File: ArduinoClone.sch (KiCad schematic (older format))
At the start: 13 parts, among them U1 DS1337, U2 24LC1025, U3 24LC1025, U4 ATMEGA328-AU, Y1 Crystal, Y2 Crystal

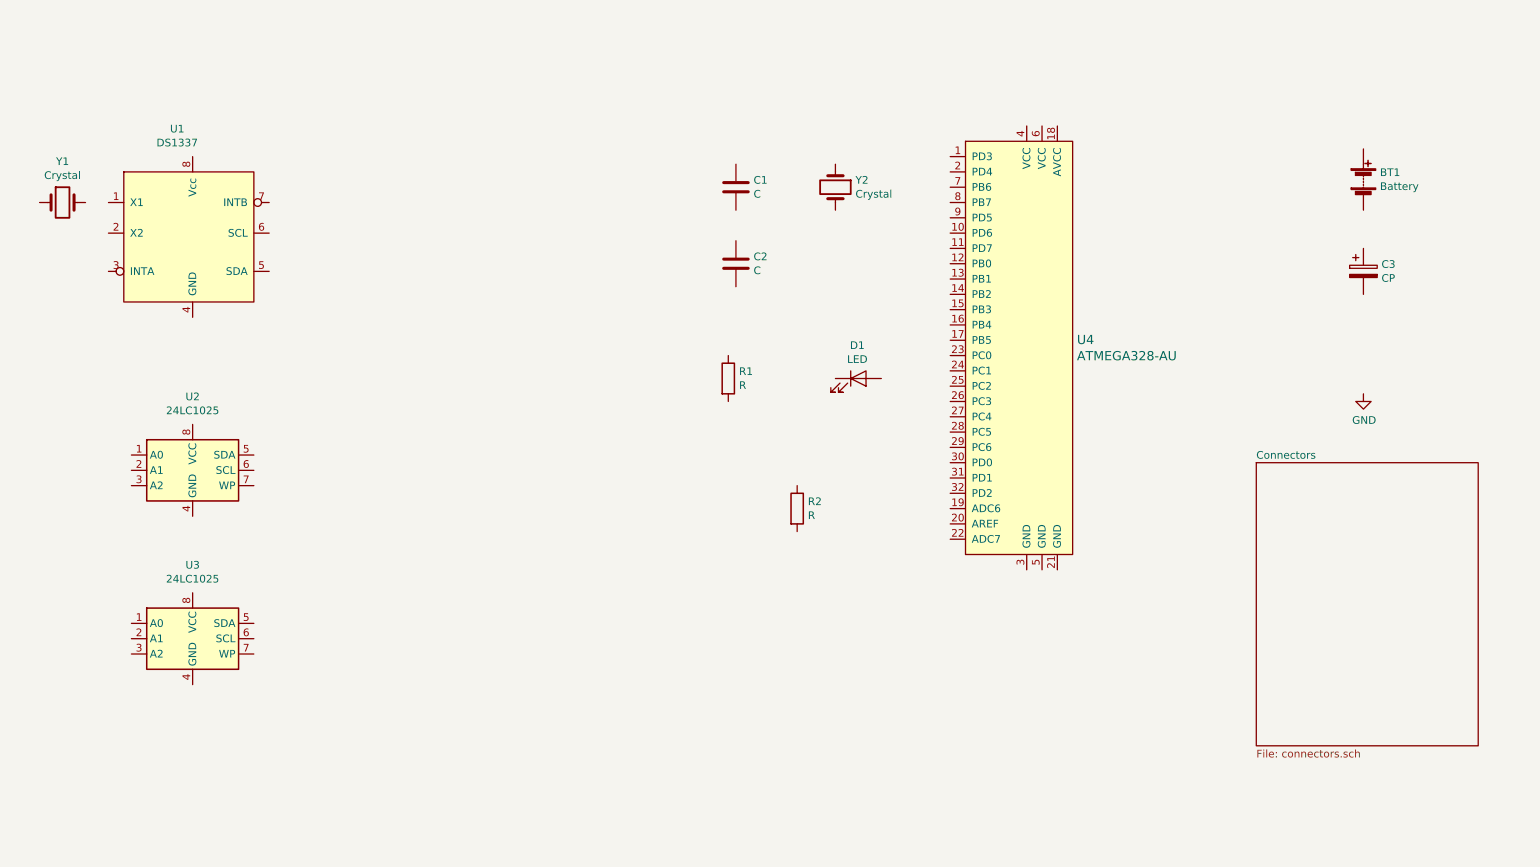
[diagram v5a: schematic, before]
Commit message: added components lables and footprints
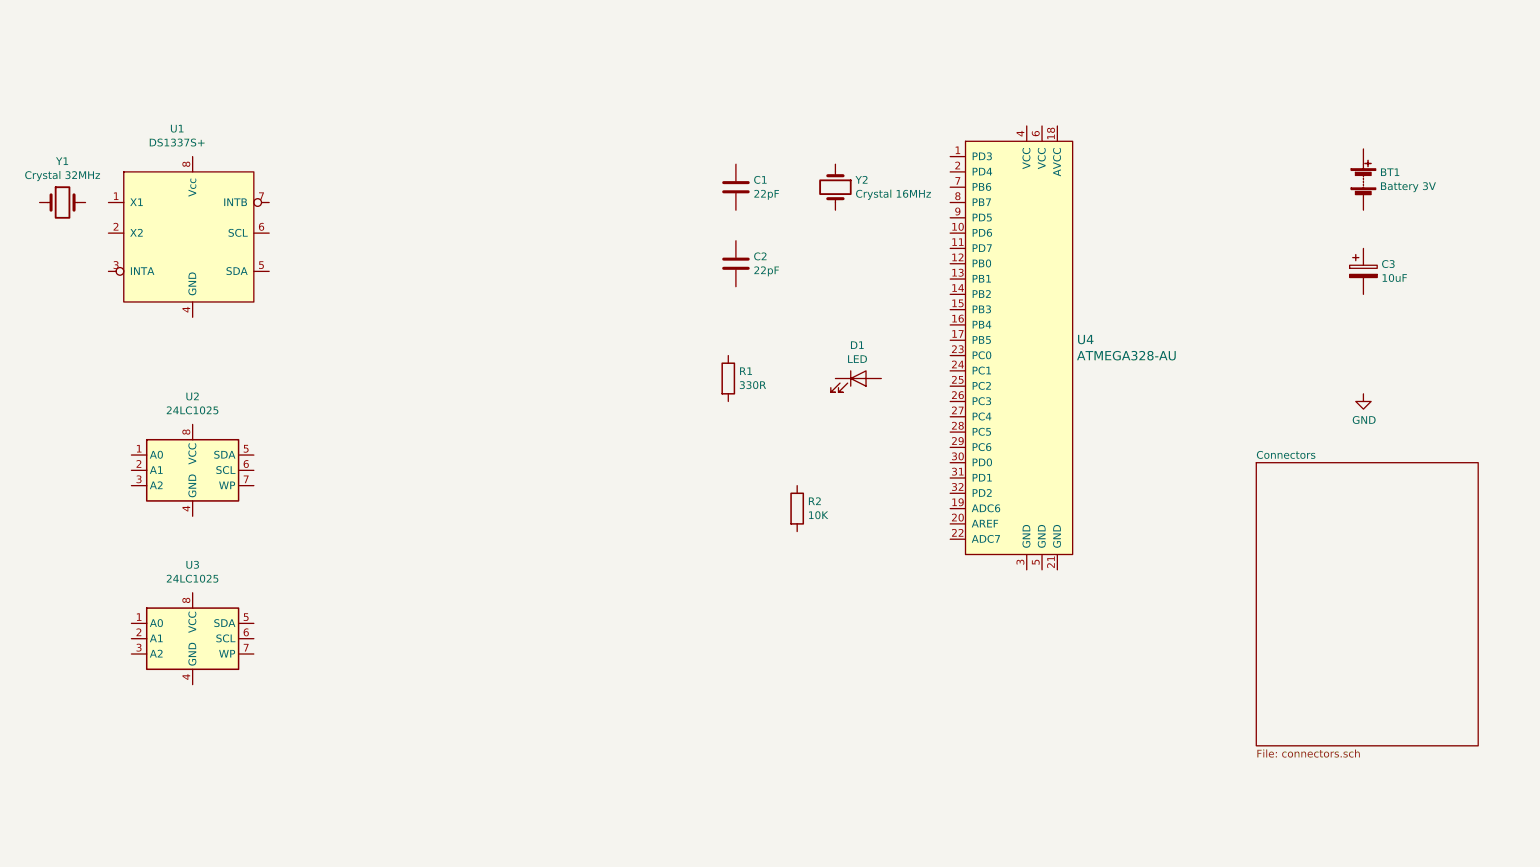
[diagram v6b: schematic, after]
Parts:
- BT1: value Battery -> Battery 3V; footprint (none) -> Connector_PinHeader_2.54mm:PinHeader_1x02_P2.54mm_Vertical
- C1, C2: value C -> 22pF; footprint (none) -> Capacitor_SMD:C_0805_2012Metric_Pad1.15x1.40mm_HandSolder
- C3: value CP -> 10uF; footprint (none) -> Capacitor_SMD:C_0805_2012Metric_Pad1.15x1.40mm_HandSolder
- D1: footprint (none) -> LED_SMD:LED_0805_2012Metric_Pad1.15x1.40mm_HandSolder
- R1: value R -> 330R; footprint (none) -> Resistor_SMD:R_0805_2012Metric_Pad1.15x1.40mm_HandSolder
- R2: value R -> 10K; footprint (none) -> Resistor_SMD:R_0805_2012Metric_Pad1.15x1.40mm_HandSolder
- U1: value DS1337 -> DS1337S+; footprint (none) -> Package_SO:SO-8_5.3x6.2mm_P1.27mm
- U2, U3: footprint (none) -> Package_SO:SOIJ-8_5.3x5.3mm_P1.27mm
- Y1: value Crystal -> Crystal 32MHz; footprint (none) -> Crystal:Crystal_SMD_MicroCrystal_CC7V-T1A-2Pin_3.2x1.5mm
- Y2: value Crystal -> Crystal 16MHz; footprint (none) -> Crystal:Crystal_SMD_5032-2Pin_5.0x3.2mm_HandSoldering
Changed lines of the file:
@@
 P 9650 2200
 F 0 "BT1" H 9758 2246 50  0000 L CNN
-F 1 "Battery" H 9758 2155 50  0000 L CNN
-F 2 "" V 9650 2260 50  0001 C CNN
+F 1 "Battery 3V" H 9758 2155 50  0000 L CNN
+F 2 "Connector_PinHeader_2.54mm:PinHeader_1x02_P2.54mm_Vertical" V 9650 2260 50  0001 C CNN
 F 3 "~" V 9650 2260 50  0001 C CNN
 	1    9650 2200
@@
 P 5550 2250
 F 0 "C1" H 5665 2296 50  0000 L CNN
-F 1 "C" H 5665 2205 50  0000 L CNN
-F 2 "" H 5588 2100 50  0001 C CNN
+F 1 "22pF" H 5665 2205 50  0000 L CNN
+F 2 "Capacitor_SMD:C_0805_2012Metric_Pad1.15x1.40mm_HandSolder" H 5588 2100 50  0001 C CNN
 F 3 "~" H 5550 2250 50  0001 C CNN
 	1    5550 2250
@@
 P 5550 2750
 F 0 "C2" H 5665 2796 50  0000 L CNN
-F 1 "C" H 5665 2705 50  0000 L CNN
-F 2 "" H 5588 2600 50  0001 C CNN
+F 1 "22pF" H 5665 2705 50  0000 L CNN
+F 2 "Capacitor_SMD:C_0805_2012Metric_Pad1.15x1.40mm_HandSolder" H 5588 2600 50  0001 C CNN
 F 3 "~" H 5550 2750 50  0001 C CNN
 	1    5550 2750
@@
 P 9650 2800
 F 0 "C3" H 9768 2846 50  0000 L CNN
-F 1 "CP" H 9768 2755 50  0000 L CNN
-F 2 "" H 9688 2650 50  0001 C CNN
+F 1 "10uF" H 9768 2755 50  0000 L CNN
+F 2 "Capacitor_SMD:C_0805_2012Metric_Pad1.15x1.40mm_HandSolder" H 9688 2650 50  0001 C CNN
 F 3 "~" H 9650 2800 50  0001 C CNN
 	1    9650 2800
@@
 F 0 "D1" H 6343 3716 50  0000 C CNN
 F 1 "LED" H 6343 3625 50  0000 C CNN
-F 2 "" H 6350 3500 50  0001 C CNN
+F 2 "LED_SMD:LED_0805_2012Metric_Pad1.15x1.40mm_HandSolder" H 6350 3500 50  0001 C CNN
 F 3 "~" H 6350 3500 50  0001 C CNN
 	1    6350 3500
@@
 P 5950 4350
 F 0 "R2" H 6020 4396 50  0000 L CNN
-F 1 "R" H 6020 4305 50  0000 L CNN
-F 2 "" V 5880 4350 50  0001 C CNN
+F 1 "10K" H 6020 4305 50  0000 L CNN
+F 2 "Resistor_SMD:R_0805_2012Metric_Pad1.15x1.40mm_HandSolder" V 5880 4350 50  0001 C CNN
 F 3 "~" H 5950 4350 50  0001 C CNN
 	1    5950 4350
@@
 P 5500 3500
 F 0 "R1" H 5570 3546 50  0000 L CNN
-F 1 "R" H 5570 3455 50  0000 L CNN
-F 2 "" V 5430 3500 50  0001 C CNN
+F 1 "330R" H 5570 3455 50  0000 L CNN
+F 2 "Resistor_SMD:R_0805_2012Metric_Pad1.15x1.40mm_HandSolder" V 5430 3500 50  0001 C CNN
 F 3 "~" H 5500 3500 50  0001 C CNN
 	1    5500 3500
@@
 F 0 "U2" H 2000 4581 50  0000 C CNN
 F 1 "24LC1025" H 2000 4490 50  0000 C CNN
-F 2 "" H 2000 4100 50  0001 C CNN
+F 2 "Package_SO:SOIJ-8_5.3x5.3mm_P1.27mm" H 2000 4100 50  0001 C CNN
 F 3 "http://ww1.microchip.com/downloads/en/DeviceDoc/21941B.pdf" H 2000 4100 50  0001 C CNN
 	1    2000 4100
@@
 P 2000 2550
 F 0 "U1" H 1899 3231 50  0000 C CNN
-F 1 "DS1337" H 1899 3140 50  0000 C CNN
-F 2 "" H 1900 2950 50  0001 C CNN
+F 1 "DS1337S+" H 1899 3140 50  0000 C CNN
+F 2 "Package_SO:SO-8_5.3x6.2mm_P1.27mm" H 1900 2950 50  0001 C CNN
 F 3 "" H 1900 2950 50  0001 C CNN
 	1    2000 2550
@@
 P 6200 2250
 F 0 "Y2" V 6154 2381 50  0000 L CNN
-F 1 "Crystal" V 6245 2381 50  0000 L CNN
-F 2 "" H 6200 2250 50  0001 C CNN
+F 1 "Crystal 16MHz" V 6245 2381 50  0000 L CNN
+F 2 "Crystal:Crystal_SMD_5032-2Pin_5.0x3.2mm_HandSoldering" H 6200 2250 50  0001 C CNN
 F 3 "~" H 6200 2250 50  0001 C CNN
 	1    6200 2250
@@
 P 1150 2350
 F 0 "Y1" H 1150 2618 50  0000 C CNN
-F 1 "Crystal" H 1150 2527 50  0000 C CNN
-F 2 "" H 1150 2350 50  0001 C CNN
+F 1 "Crystal 32MHz" H 1150 2527 50  0000 C CNN
+F 2 "Crystal:Crystal_SMD_MicroCrystal_CC7V-T1A-2Pin_3.2x1.5mm" H 1150 2350 50  0001 C CNN
 F 3 "~" H 1150 2350 50  0001 C CNN
 	1    1150 2350
@@
 F 0 "U3" H 2000 5681 50  0000 C CNN
 F 1 "24LC1025" H 2000 5590 50  0000 C CNN
-F 2 "" H 2000 5200 50  0001 C CNN
+F 2 "Package_SO:SOIJ-8_5.3x5.3mm_P1.27mm" H 2000 5200 50  0001 C CNN
 F 3 "http://ww1.microchip.com/downloads/en/DeviceDoc/21941B.pdf" H 2000 5200 50  0001 C CNN
 	1    2000 5200

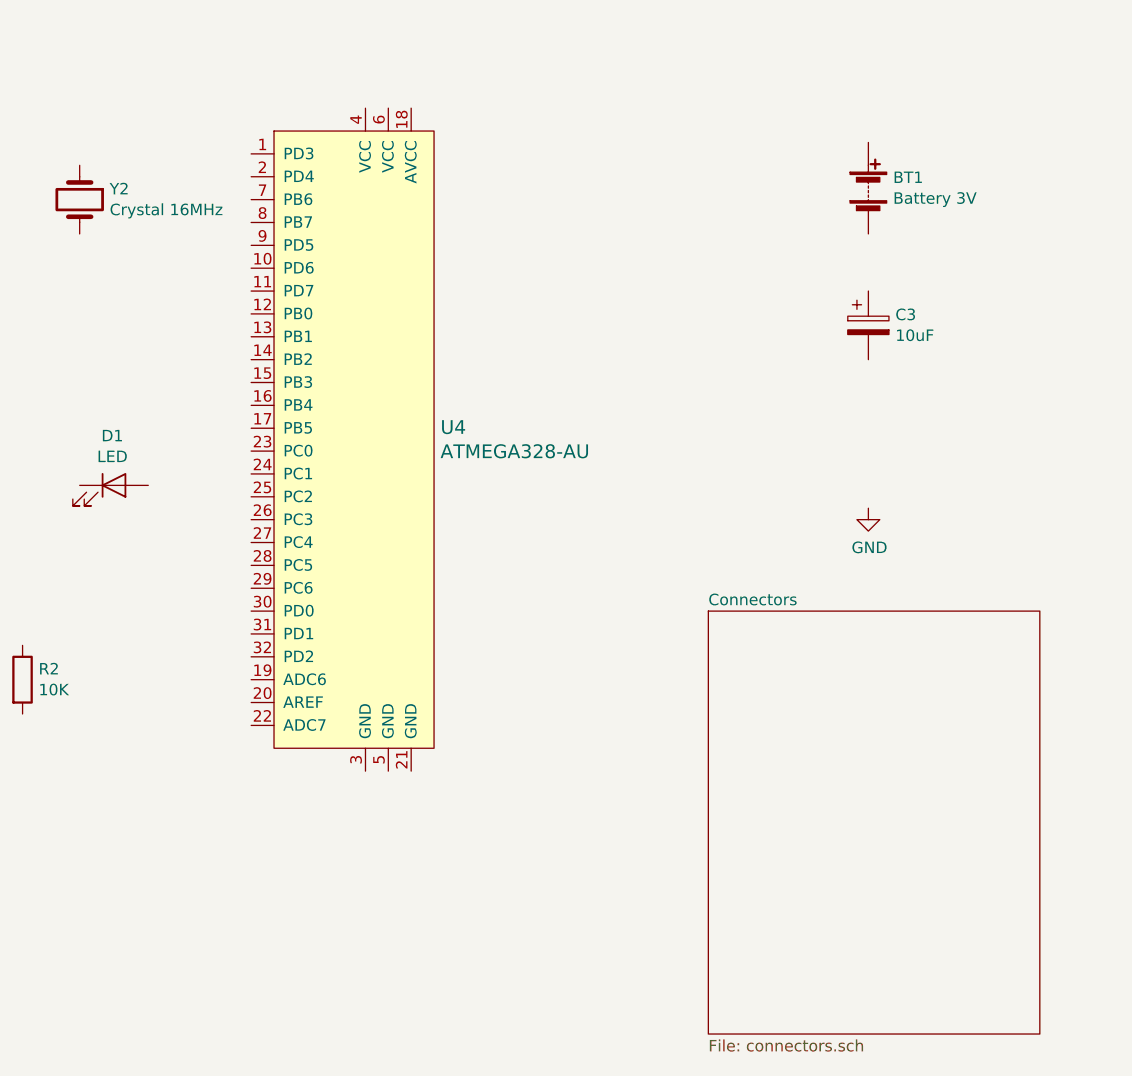
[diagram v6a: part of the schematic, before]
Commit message: Completed wiring in the connectors sheet
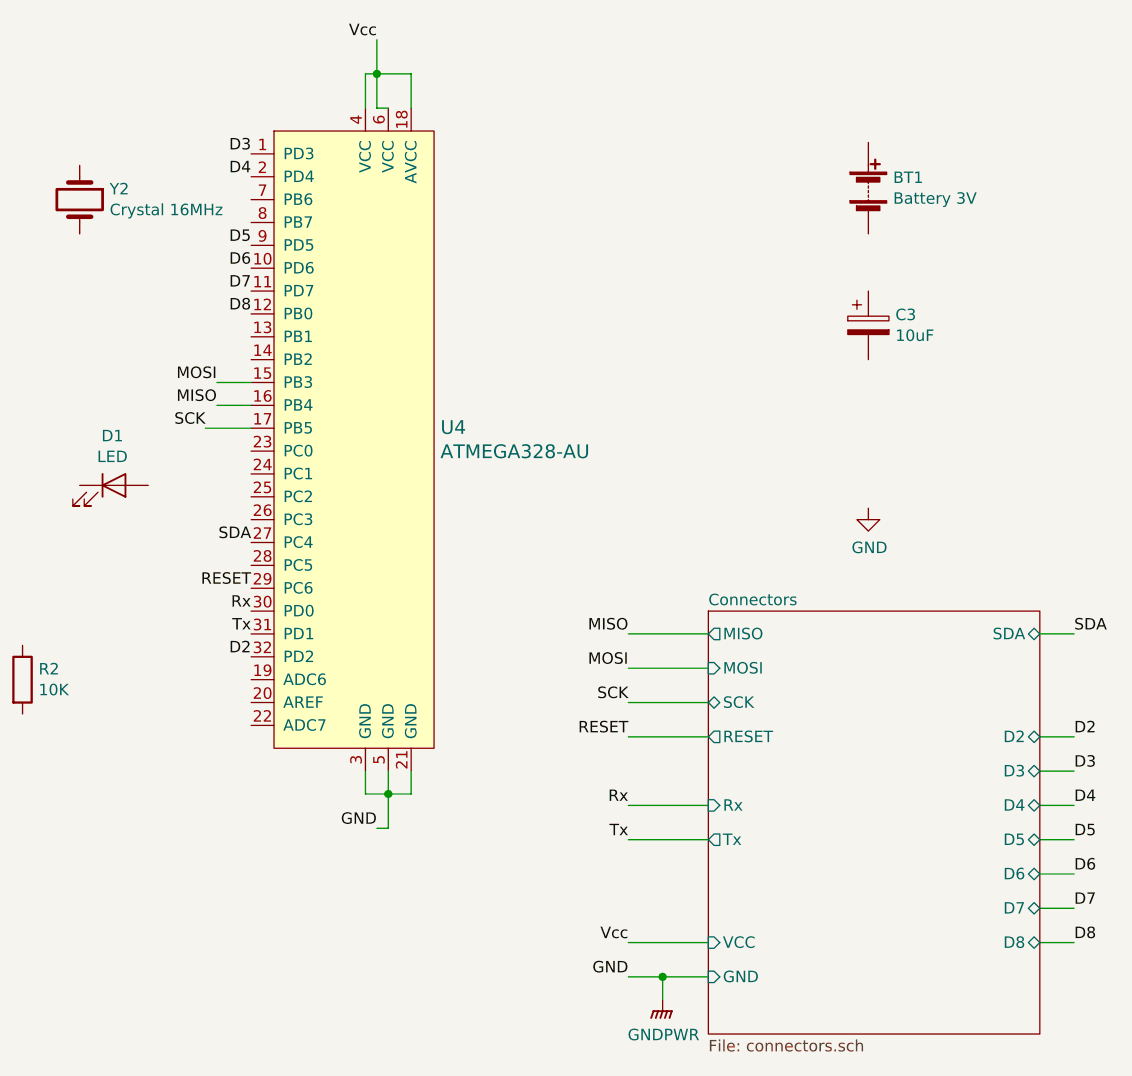
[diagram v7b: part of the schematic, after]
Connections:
- net GND: now also U4.21 (GND), U4.3 (GND), U4.5 (GND)
- net D3: now reaches U4.1 (PD3)
- net D6: now reaches U4.10 (PD6)
- net D7: now reaches U4.11 (PD7)
- net D8: now reaches U4.12 (PB0)
- net MOSI: now reaches U4.15 (PB3)
- net MISO: now reaches U4.16 (PB4)
- net SCK: now reaches U4.17 (PB5)
- net Vcc: now reaches U4.18 (AVCC)
- net Vcc: now also U4.4 (VCC), U4.6 (VCC)
- net D4: now reaches U4.2 (PD4)
- net SDA: now reaches U4.27 (PC4)
- net RESET: now reaches U4.29 (PC6)
- net Rx: now reaches U4.30 (PD0)
- net Tx: now reaches U4.31 (PD1)
- net D2: now reaches U4.32 (PD2)
- net D5: now reaches U4.9 (PD5)
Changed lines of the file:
@@
 F0 "Connectors" 50
 F1 "connectors.sch" 50
+F2 "MISO" O L 8950 4150 50
+F3 "SCK" B L 8950 4450 50
+F4 "RESET" O L 8950 4600 50
+F5 "VCC" I L 8950 5500 50
+F6 "MOSI" I L 8950 4300 50
+F7 "GND" I L 8950 5650 50
+F8 "Rx" I L 8950 4900 50
+F9 "Tx" O L 8950 5050 50
+F10 "SDA" B R 10400 4150 50
+F11 "D2" B R 10400 4600 50
+F12 "D3" B R 10400 4750 50
+F13 "D4" B R 10400 4900 50
+F14 "D5" B R 10400 5050 50
+F15 "D6" B R 10400 5200 50
+F16 "D7" B R 10400 5350 50
+F17 "D8" B R 10400 5500 50
 $EndSheet
 $Comp
@@
 	1    0    0    -1
 $EndComp
+Text Label 8600 4150 2    50   ~ 0
+MISO
+Wire Wire Line
+	8600 4150 8950 4150
+Text Label 6800 3150 2    50   ~ 0
+MISO
+Wire Wire Line
+	6800 3150 6950 3150
+Text Label 8600 4450 2    50   ~ 0
+SCK
+Wire Wire Line
+	8600 4450 8950 4450
+Text Label 8600 4600 2    50   ~ 0
+RESET
+Text Label 8600 5500 2    50   ~ 0
+Vcc
+Text Label 8600 4300 2    50   ~ 0
+MOSI
+Text Label 8600 5650 2    50   ~ 0
+GND
+Wire Wire Line
+	8600 4600 8950 4600
+Wire Wire Line
+	8600 5500 8950 5500
+Wire Wire Line
+	8600 4300 8950 4300
+Wire Wire Line
+	8600 5650 8750 5650
+Text Label 6800 3050 2    50   ~ 0
+MOSI
+Wire Wire Line
+	6800 3050 6950 3050
+Text Label 6750 3250 2    50   ~ 0
+SCK
+Wire Wire Line
+	6750 3250 6950 3250
+Text Label 7500 1550 2    50   ~ 0
+Vcc
+Wire Wire Line
+	7500 1550 7500 1700
+Wire Wire Line
+	7500 1700 7650 1700
+Wire Wire Line
+	7650 1700 7650 1850
+Wire Wire Line
+	7500 1700 7450 1700
+Wire Wire Line
+	7450 1700 7450 1850
+Connection ~ 7500 1700
+Wire Wire Line
+	7500 1700 7500 1850
+Wire Wire Line
+	7500 1850 7550 1850
+Text Label 6950 3950 2    50   ~ 0
+RESET
+Text Label 7500 5000 2    50   ~ 0
+GND
+Wire Wire Line
+	7550 4750 7550 4850
+Wire Wire Line
+	7550 5000 7500 5000
+Wire Wire Line
+	7450 4750 7450 4850
+Wire Wire Line
+	7450 4850 7550 4850
+Connection ~ 7550 4850
+Wire Wire Line
+	7550 4850 7550 5000
+Wire Wire Line
+	7650 4750 7650 4850
+Wire Wire Line
+	7650 4850 7550 4850
+$Comp
+L power:GNDPWR #PWR?
+U 1 1 5E9DFB73
+P 8750 5750
+F 0 "#PWR?" H 8750 5550 50  0001 C CNN
+F 1 "GNDPWR" H 8754 5596 50  0000 C CNN
+F 2 "" H 8750 5700 50  0001 C CNN
+F 3 "" H 8750 5700 50  0001 C CNN
+	1    8750 5750
+	1    0    0    -1
+$EndComp
+Wire Wire Line
+	8750 5750 8750 5650
+Connection ~ 8750 5650
+Wire Wire Line
+	8750 5650 8950 5650
+Text Label 10550 4150 0    50   ~ 0
+SDA
+Text Label 10550 4600 0    50   ~ 0
+D2
+Text Label 10550 4750 0    50   ~ 0
+D3
+Text Label 10550 4900 0    50   ~ 0
+D4
+Text Label 10550 5050 0    50   ~ 0
+D5
+Text Label 10550 5200 0    50   ~ 0
+D6
+Text Label 10550 5350 0    50   ~ 0
+D7
+Text Label 10550 5500 0    50   ~ 0
+D8
+Text Label 8600 5050 2    50   ~ 0
+Tx
+Text Label 8600 4900 2    50   ~ 0
+Rx
+Wire Wire Line
+	10550 4150 10400 4150
+Wire Wire Line
+	10550 4600 10400 4600
+Wire Wire Line
+	10550 4750 10400 4750
+Wire Wire Line
+	10550 4900 10400 4900
+Wire Wire Line
+	10550 5050 10400 5050
+Wire Wire Line
+	10550 5200 10400 5200
+Wire Wire Line
+	10550 5350 10400 5350
+Wire Wire Line
+	10550 5500 10400 5500
+Wire Wire Line
+	8600 4900 8950 4900
+Wire Wire Line
+	8600 5050 8950 5050
+Text Label 6950 2050 2    50   ~ 0
+D3
+Text Label 6950 2150 2    50   ~ 0
+D4
+Text Label 6950 2450 2    50   ~ 0
+D5
+Text Label 6950 2550 2    50   ~ 0
+D6
+Text Label 6950 2650 2    50   ~ 0
+D7
+Text Label 6950 2750 2    50   ~ 0
+D8
+Text Label 6950 3750 2    50   ~ 0
+SDA
+Text Label 6950 4050 2    50   ~ 0
+Rx
+Text Label 6950 4150 2    50   ~ 0
+Tx
+Text Label 6950 4250 2    50   ~ 0
+D2
 $EndSCHEMATC
